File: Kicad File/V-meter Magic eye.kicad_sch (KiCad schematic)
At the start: 49 parts, among them J1 15V, J2 VT138 socket, J3 BF IN, J4 VT138 socket, Q1 IRFBG 30, Q2 BC547, Q3 BC547, Q4 BC547, U1 NE555P, U5 VT138

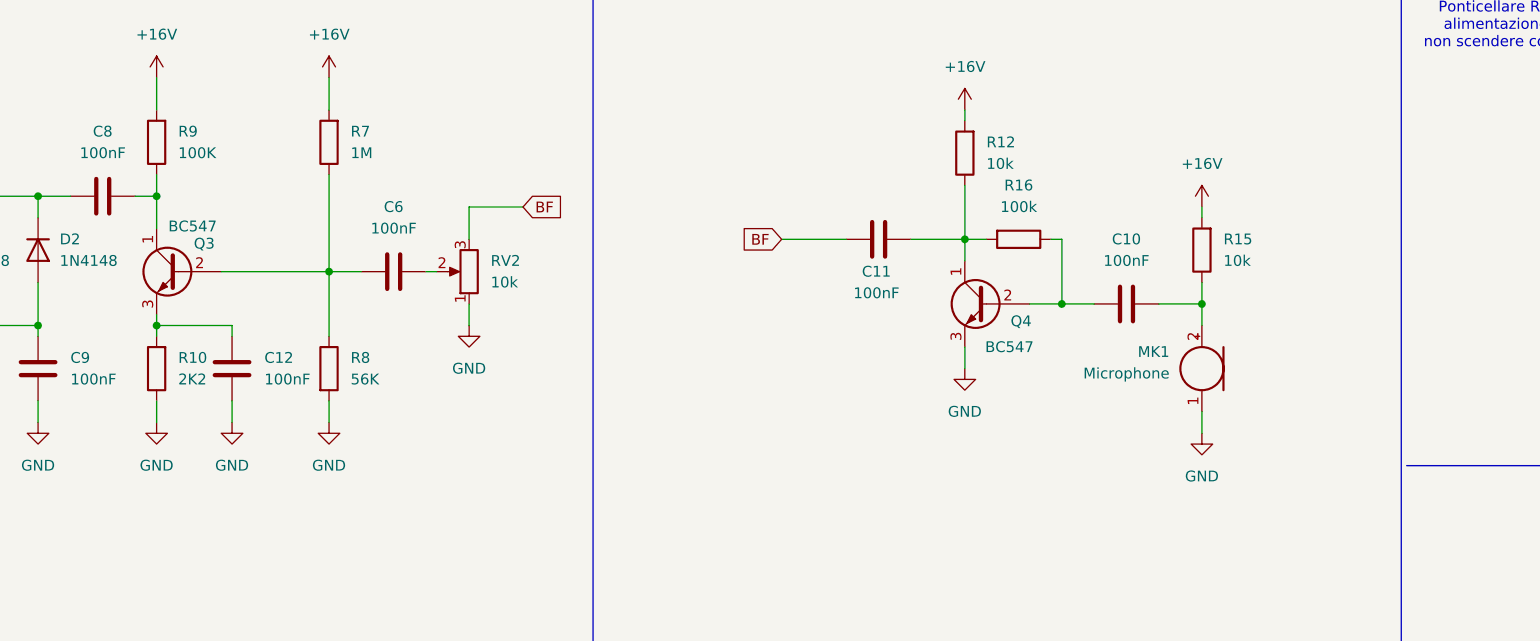
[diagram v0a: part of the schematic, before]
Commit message: V1.3
inserito capacità riuzione rumore alimentazione
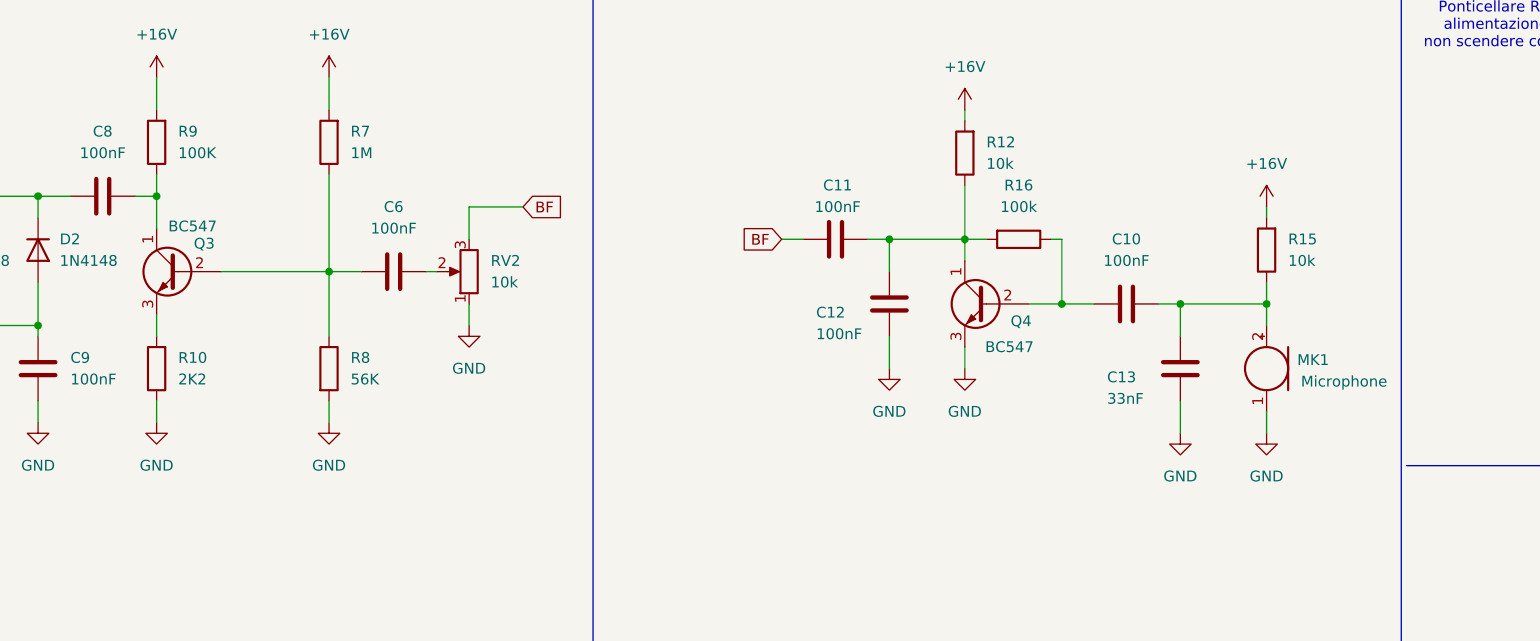
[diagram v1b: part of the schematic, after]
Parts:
- added C13: 33nF, Capacitor_THT:C_Rect_L7.0mm_W2.5mm_P5.00mm, symbol Device:C
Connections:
- net GND: now also C13.1
- net at C10.2, MK1.2 (+), R15.1: now also C13.2
- net at C11.2, Q4.1 (C), R12.1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: now also C12.2
- net at Q3.3 (E), R10.2: no longer C12.2
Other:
- moved on the sheet: C11, MK1, R15
